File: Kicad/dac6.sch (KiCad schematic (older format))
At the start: 13 parts

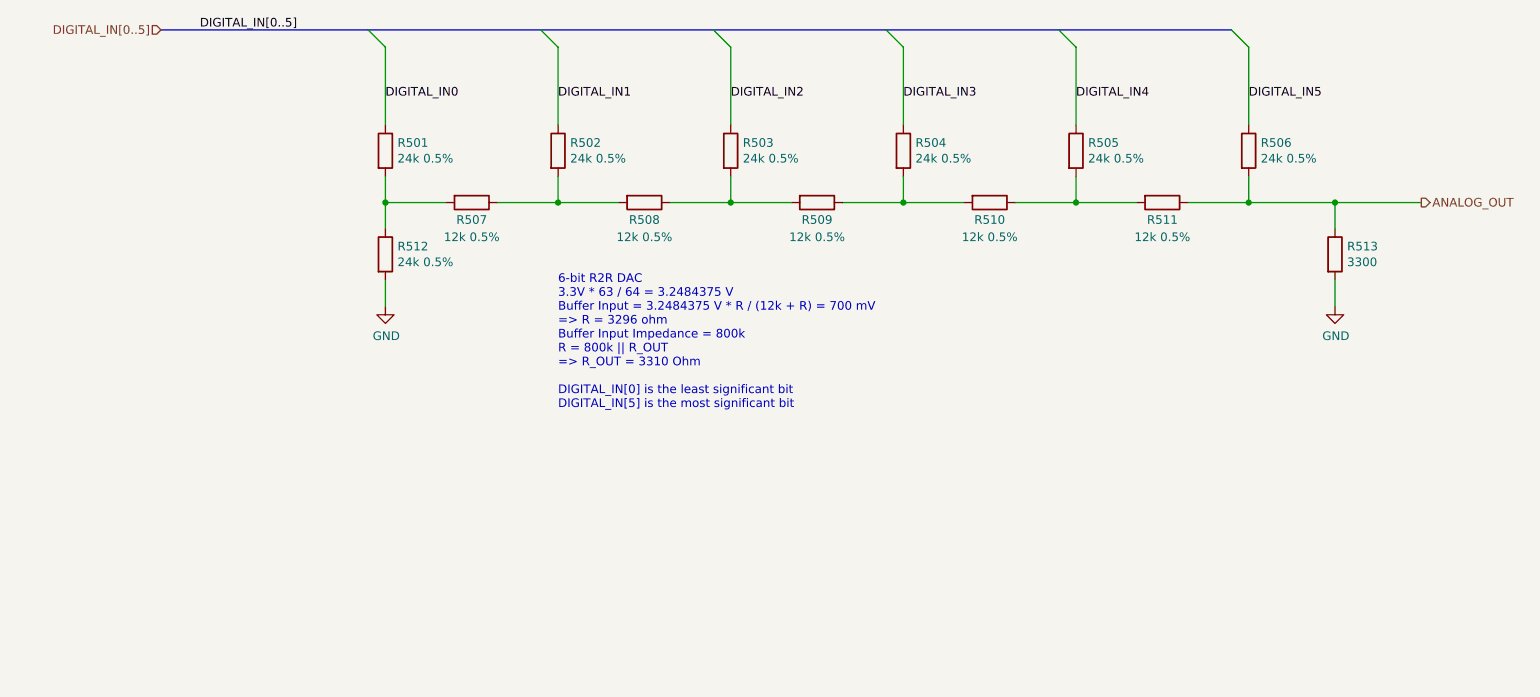
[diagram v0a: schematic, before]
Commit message: Added 12-bit video DAC.
Also had to change footprints to suit Kicad 5.1.9
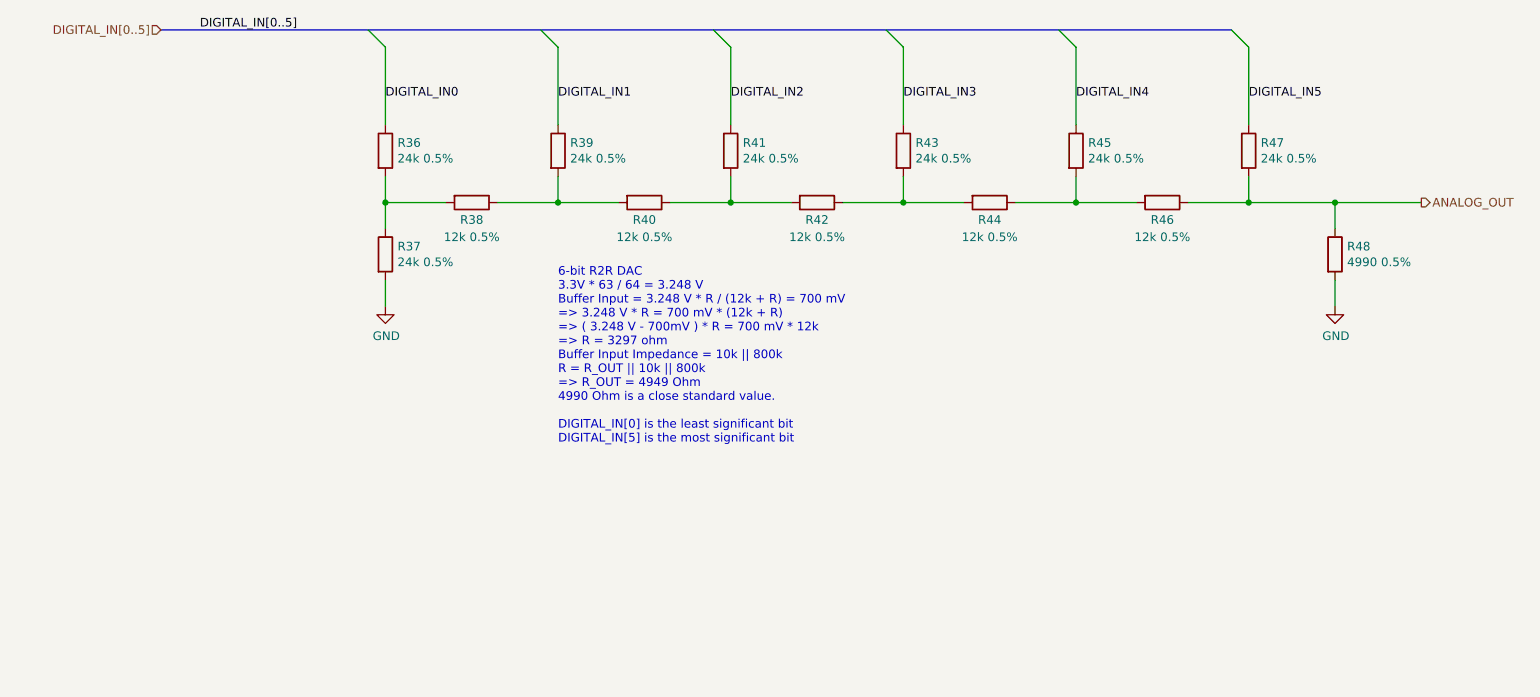
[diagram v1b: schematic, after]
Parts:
- removed R301, R304: 24k 0.5%, Resistor_SMD:R_0805_2012Metric_Pad1.15x1.40mm_HandSolder, symbol Device:R
- added R23, R30: 24k 0.5%, Resistor_SMD:R_0805_2012Metric_Pad1.20x1.40mm_HandSolder, symbol Device:R
- R24: renamed from R312; footprint Resistor_SMD:R_0805_2012Metric_Pad1.15x1.40mm_HandSolder -> Resistor_SMD:R_0805_2012Metric_Pad1.20x1.40mm_HandSolder
- R25: renamed from R307; footprint Resistor_SMD:R_0805_2012Metric_Pad1.15x1.40mm_HandSolder -> Resistor_SMD:R_0805_2012Metric_Pad1.20x1.40mm_HandSolder
- R26: renamed from R302; footprint Resistor_SMD:R_0805_2012Metric_Pad1.15x1.40mm_HandSolder -> Resistor_SMD:R_0805_2012Metric_Pad1.20x1.40mm_HandSolder
- R27: renamed from R308; footprint Resistor_SMD:R_0805_2012Metric_Pad1.15x1.40mm_HandSolder -> Resistor_SMD:R_0805_2012Metric_Pad1.20x1.40mm_HandSolder
- R28: renamed from R303; footprint Resistor_SMD:R_0805_2012Metric_Pad1.15x1.40mm_HandSolder -> Resistor_SMD:R_0805_2012Metric_Pad1.20x1.40mm_HandSolder
- R29: renamed from R309; footprint Resistor_SMD:R_0805_2012Metric_Pad1.15x1.40mm_HandSolder -> Resistor_SMD:R_0805_2012Metric_Pad1.20x1.40mm_HandSolder
- R31: renamed from R310; footprint Resistor_SMD:R_0805_2012Metric_Pad1.15x1.40mm_HandSolder -> Resistor_SMD:R_0805_2012Metric_Pad1.20x1.40mm_HandSolder
- R32: renamed from R305; footprint Resistor_SMD:R_0805_2012Metric_Pad1.15x1.40mm_HandSolder -> Resistor_SMD:R_0805_2012Metric_Pad1.20x1.40mm_HandSolder
- R33: renamed from R311; footprint Resistor_SMD:R_0805_2012Metric_Pad1.15x1.40mm_HandSolder -> Resistor_SMD:R_0805_2012Metric_Pad1.20x1.40mm_HandSolder
- R34: renamed from R306; footprint Resistor_SMD:R_0805_2012Metric_Pad1.15x1.40mm_HandSolder -> Resistor_SMD:R_0805_2012Metric_Pad1.20x1.40mm_HandSolder
- R35: renamed from R313; value 3300 -> 4990 0.5%; footprint Resistor_SMD:R_0805_2012Metric_Pad1.15x1.40mm_HandSolder -> Resistor_SMD:R_0805_2012Metric_Pad1.20x1.40mm_HandSolder
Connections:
- net DIGITAL_IN0: now also R23.1
- net DIGITAL_IN3: now also R30.1
- net at R24.1, R25.2: now also R23.2
- net at R29.1, R31.2: now also R30.2
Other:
- note added: "6-bit R2R DAC\n3.3V * 63 / 64 = 3.248 V\nBuffer Input = 3.248 V * R / (12k + R) = 700 mV\n=> 3.248 V * R = 700 mV * (12k + R)\n=> ( 3.248 V - 700mV ) * R = 700 mV * 12k\n=> R = 3297 ohm\nBuffer Input Impedance = 10k || 800k\nR = R_OUT || 10k || 800k\n=> R_OUT = 4949 Ohm\n4990 Ohm is a close standard value.\n\nDIGITAL_IN[0] is the least significant bit\nDIGITAL_IN[5] is the most significant bit\n"
- note removed: "6-bit R2R DAC\n3.3V * 63 / 64 = 3.2484375 V\nBuffer Input = 3.2484375 V * R / (12k + R) = 700 mV\n=> R = 3296 ohm\nBuffer Input Impedance = 800k\nR = 800k || R_OUT\n=> R_OUT = 3310 Ohm\n\nDIGITAL_IN[0] is the least significant bit\nDIGITAL_IN[5] is the most significant bit\n"

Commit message: Add 4-bit Video DAC, and re-wire BMC.
Now the BMC is an SPI device, and has a four-wire UART.
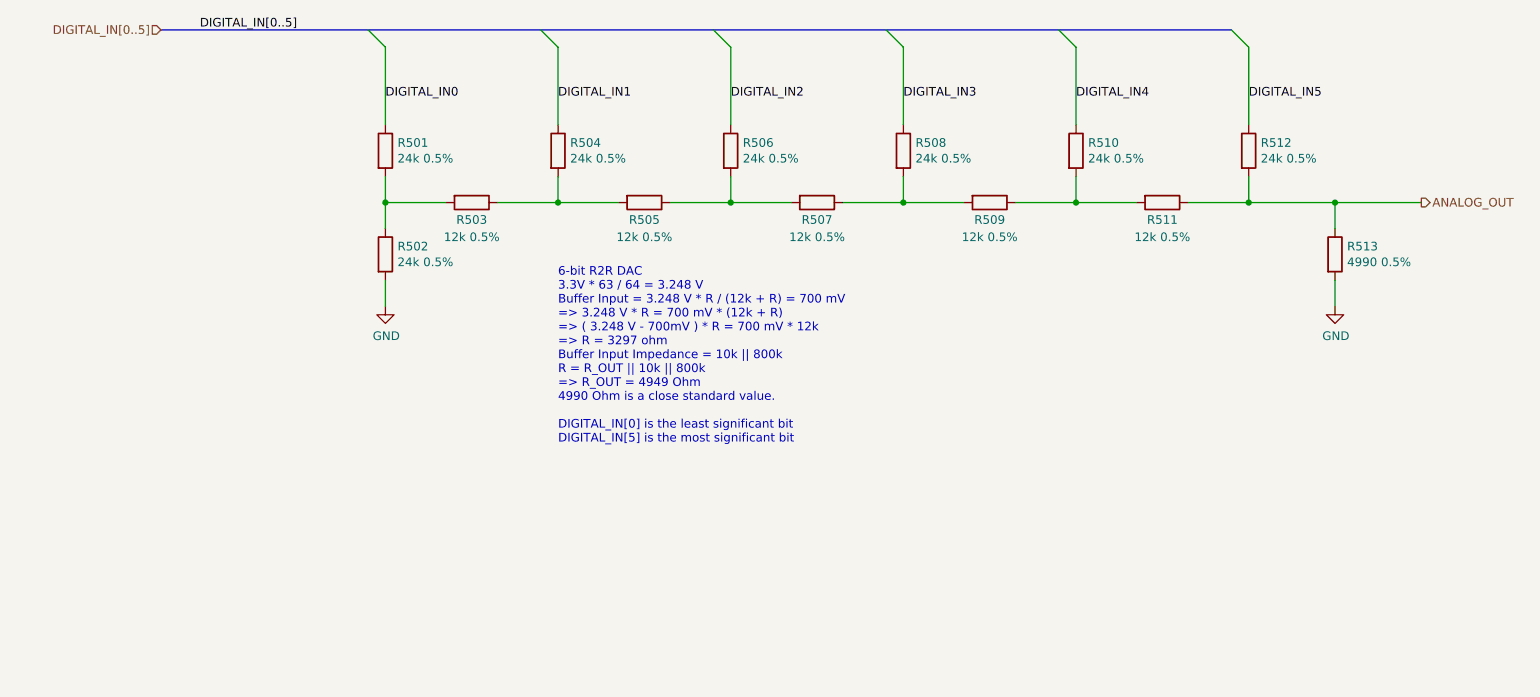
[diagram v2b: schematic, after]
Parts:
- renumbered R23 to R401, R24 to R402, R25 to R403, R26 to R404, R27 to R405, R28 to R406, R29 to R407, R30 to R408, R31 to R409, R32 to R410, R33 to R411, R34 to R412, R35 to R413

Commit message: Tidy up part nos and swapped I2C/UART on BMC.
Mark all resistors as 1% if not specified.
Added some Mouser part numbers.
BMC can now be programmed over UART.
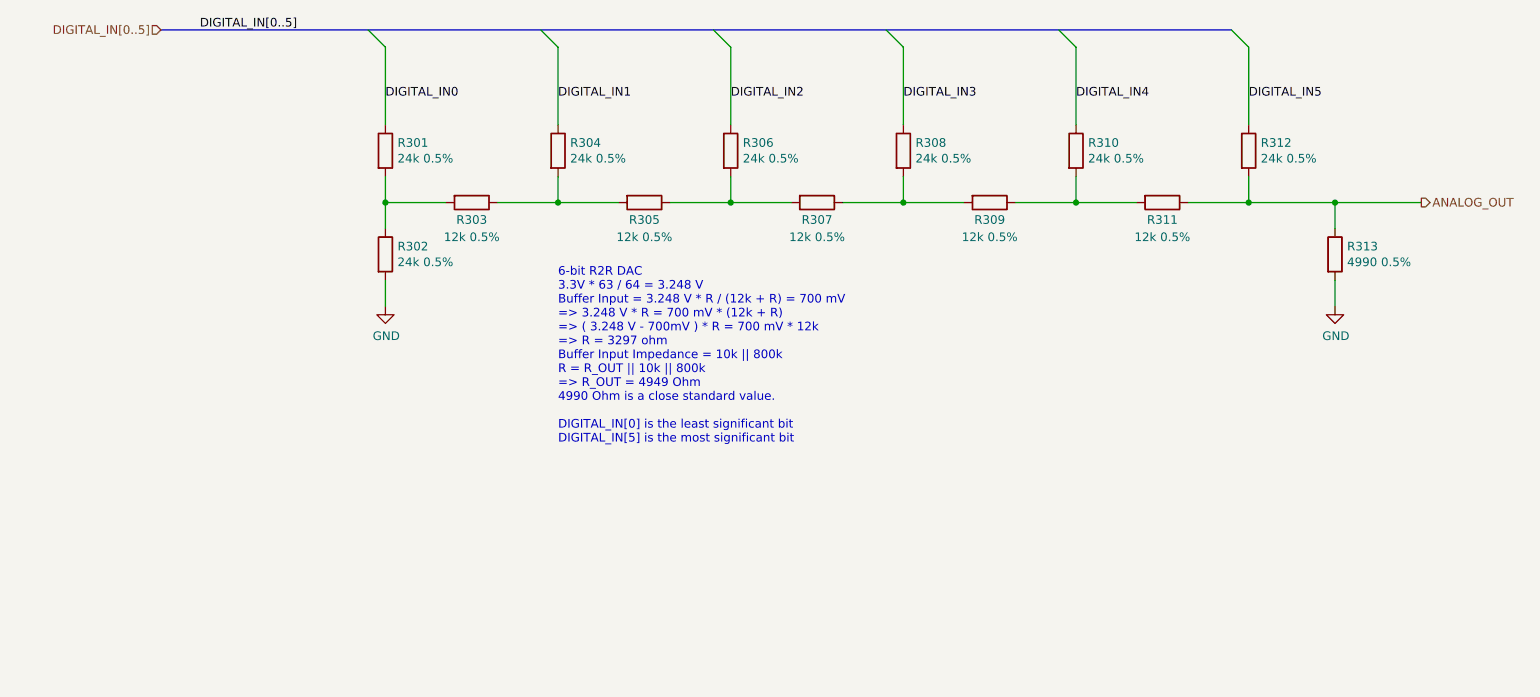
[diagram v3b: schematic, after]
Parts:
- R413: Digikey RMCF0805FG3K30-ND -> RNCF0805DTE4K99CT-ND; MPN RMCF0805FG3K30 -> RNCF0805DTE4K99
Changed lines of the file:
@@
 AR Path="/5FDE658D/60682025/60681FF8" Ref="R301"  Part="1"
 AR Path="/5FDE658D/6068202F/60681FF8" Ref="R501"  Part="1"
-F 0 "R501" H 3570 2746 50  0000 L CNN
+F 0 "R301" H 3570 2746 50  0000 L CNN
 F 1 "24k 0.5%" H 3570 2655 50  0000 L CNN
 F 2 "Resistor_SMD:R_0805_2012Metric_Pad1.20x1.40mm_HandSolder" V 3430 2700 50  0001 C CNN
@@
 AR Path="/5FDE658D/60682025/5F5F5C61" Ref="R303"  Part="1"
 AR Path="/5FDE658D/6068202F/5F5F5C61" Ref="R503"  Part="1"
-F 0 "R503" V 4100 3000 50  0000 C CNN
+F 0 "R303" V 4100 3000 50  0000 C CNN
 F 1 "12k 0.5%" V 4200 3000 50  0000 C CNN
 F 2 "Resistor_SMD:R_0805_2012Metric_Pad1.20x1.40mm_HandSolder" V 3930 3000 50  0001 C CNN
@@
 AR Path="/5FDE658D/60682025/5F5F6568" Ref="R304"  Part="1"
 AR Path="/5FDE658D/6068202F/5F5F6568" Ref="R504"  Part="1"
-F 0 "R504" H 4570 2746 50  0000 L CNN
+F 0 "R304" H 4570 2746 50  0000 L CNN
 F 1 "24k 0.5%" H 4570 2655 50  0000 L CNN
 F 2 "Resistor_SMD:R_0805_2012Metric_Pad1.20x1.40mm_HandSolder" V 4430 2700 50  0001 C CNN
@@
 AR Path="/5FDE658D/60682025/5F5F6D42" Ref="R305"  Part="1"
 AR Path="/5FDE658D/6068202F/5F5F6D42" Ref="R505"  Part="1"
-F 0 "R505" V 5100 3000 50  0000 C CNN
+F 0 "R305" V 5100 3000 50  0000 C CNN
 F 1 "12k 0.5%" V 5200 3000 50  0000 C CNN
 F 2 "Resistor_SMD:R_0805_2012Metric_Pad1.20x1.40mm_HandSolder" V 4930 3000 50  0001 C CNN
@@
 AR Path="/5FDE658D/60682025/5F5F6F45" Ref="R307"  Part="1"
 AR Path="/5FDE658D/6068202F/5F5F6F45" Ref="R507"  Part="1"
-F 0 "R507" V 6100 3000 50  0000 C CNN
+F 0 "R307" V 6100 3000 50  0000 C CNN
 F 1 "12k 0.5%" V 6200 3000 50  0000 C CNN
 F 2 "Resistor_SMD:R_0805_2012Metric_Pad1.20x1.40mm_HandSolder" V 5930 3000 50  0001 C CNN
@@
 AR Path="/5FDE658D/60682025/5F5F984D" Ref="R309"  Part="1"
 AR Path="/5FDE658D/6068202F/5F5F984D" Ref="R509"  Part="1"
-F 0 "R509" V 7100 3000 50  0000 C CNN
+F 0 "R309" V 7100 3000 50  0000 C CNN
 F 1 "12k 0.5%" V 7200 3000 50  0000 C CNN
 F 2 "Resistor_SMD:R_0805_2012Metric_Pad1.20x1.40mm_HandSolder" V 6930 3000 50  0001 C CNN
@@
 AR Path="/5FDE658D/60682025/5F5F99D6" Ref="R311"  Part="1"
 AR Path="/5FDE658D/6068202F/5F5F99D6" Ref="R511"  Part="1"
-F 0 "R511" V 8100 3000 50  0000 C CNN
+F 0 "R311" V 8100 3000 50  0000 C CNN
 F 1 "12k 0.5%" V 8200 3000 50  0000 C CNN
 F 2 "Resistor_SMD:R_0805_2012Metric_Pad1.20x1.40mm_HandSolder" V 7930 3000 50  0001 C CNN
@@
 AR Path="/5FDE658D/60682025/5F5FA2EE" Ref="R313"  Part="1"
 AR Path="/5FDE658D/6068202F/5F5FA2EE" Ref="R513"  Part="1"
-F 0 "R513" H 9070 3346 50  0000 L CNN
+F 0 "R313" H 9070 3346 50  0000 L CNN
 F 1 "4990 0.5%" H 9070 3255 50  0000 L CNN
 F 2 "Resistor_SMD:R_0805_2012Metric_Pad1.20x1.40mm_HandSolder" V 8930 3300 50  0001 C CNN
 F 3 "~" H 9000 3300 50  0001 C CNN
 F 4 "0" H 9000 3300 50  0001 C CNN "DNP"
-F 5 "RMCF0805FG3K30-ND" H 9000 3300 50  0001 C CNN "Digikey"
-F 6 "RMCF0805FG3K30" H 9000 3300 50  0001 C CNN "MPN"
+F 5 "RNCF0805DTE4K99CT-ND" H 9000 3300 50  0001 C CNN "Digikey"
+F 6 "RNCF0805DTE4K99" H 9000 3300 50  0001 C CNN "MPN"
 F 7 "Stackpole" H 9000 3300 50  0001 C CNN "Manufacturer"
 	1    9000 3300
@@
 AR Path="/5FDE658D/60682025/5F5FBB89" Ref="#PWR0301"  Part="1"
 AR Path="/5FDE658D/6068202F/5F5FBB89" Ref="#PWR0501"  Part="1"
-F 0 "#PWR0501" H 3500 3350 50  0001 C CNN
+F 0 "#PWR0301" H 3500 3350 50  0001 C CNN
 F 1 "GND" H 3505 3427 50  0000 C CNN
 F 2 "" H 3500 3600 50  0001 C CNN
@@
 AR Path="/5FDE658D/60682025/5F5FBF42" Ref="#PWR0302"  Part="1"
 AR Path="/5FDE658D/6068202F/5F5FBF42" Ref="#PWR0502"  Part="1"
-F 0 "#PWR0502" H 9000 3350 50  0001 C CNN
+F 0 "#PWR0302" H 9000 3350 50  0001 C CNN
 F 1 "GND" H 9005 3427 50  0000 C CNN
 F 2 "" H 9000 3600 50  0001 C CNN
@@
 AR Path="/5FDE658D/60682025/5F5FCF8C" Ref="R302"  Part="1"
 AR Path="/5FDE658D/6068202F/5F5FCF8C" Ref="R502"  Part="1"
-F 0 "R502" H 3570 3346 50  0000 L CNN
+F 0 "R302" H 3570 3346 50  0000 L CNN
 F 1 "24k 0.5%" H 3570 3255 50  0000 L CNN
 F 2 "Resistor_SMD:R_0805_2012Metric_Pad1.20x1.40mm_HandSolder" V 3430 3300 50  0001 C CNN
@@
 AR Path="/5FDE658D/60682025/5F5FD13B" Ref="R306"  Part="1"
 AR Path="/5FDE658D/6068202F/5F5FD13B" Ref="R506"  Part="1"
-F 0 "R506" H 5570 2746 50  0000 L CNN
+F 0 "R306" H 5570 2746 50  0000 L CNN
 F 1 "24k 0.5%" H 5570 2655 50  0000 L CNN
 F 2 "Resistor_SMD:R_0805_2012Metric_Pad1.20x1.40mm_HandSolder" V 5430 2700 50  0001 C CNN
@@
 AR Path="/5FDE658D/60682025/60682004" Ref="R308"  Part="1"
 AR Path="/5FDE658D/6068202F/60682004" Ref="R508"  Part="1"
-F 0 "R508" H 6570 2746 50  0000 L CNN
+F 0 "R308" H 6570 2746 50  0000 L CNN
 F 1 "24k 0.5%" H 6570 2655 50  0000 L CNN
 F 2 "Resistor_SMD:R_0805_2012Metric_Pad1.20x1.40mm_HandSolder" V 6430 2700 50  0001 C CNN
@@
 AR Path="/5FDE658D/60682025/5F5FD46F" Ref="R310"  Part="1"
 AR Path="/5FDE658D/6068202F/5F5FD46F" Ref="R510"  Part="1"
-F 0 "R510" H 7570 2746 50  0000 L CNN
+F 0 "R310" H 7570 2746 50  0000 L CNN
 F 1 "24k 0.5%" H 7570 2655 50  0000 L CNN
 F 2 "Resistor_SMD:R_0805_2012Metric_Pad1.20x1.40mm_HandSolder" V 7430 2700 50  0001 C CNN
@@
 AR Path="/5FDE658D/60682025/5F5FD6C1" Ref="R312"  Part="1"
 AR Path="/5FDE658D/6068202F/5F5FD6C1" Ref="R512"  Part="1"
-F 0 "R512" H 8570 2746 50  0000 L CNN
+F 0 "R312" H 8570 2746 50  0000 L CNN
 F 1 "24k 0.5%" H 8570 2655 50  0000 L CNN
 F 2 "Resistor_SMD:R_0805_2012Metric_Pad1.20x1.40mm_HandSolder" V 8430 2700 50  0001 C CNN
